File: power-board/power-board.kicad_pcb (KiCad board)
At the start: 2 copper layers, 87.5 x 37.1 mm, 7 parts, among them J1 Conn_01x04_Female, J2 Conn_02x08_Odd_Even, J3 Conn_02x08_Odd_Even, J4 Conn_02x08_Odd_Even, J5 Conn_02x08_Odd_Even, J6 Conn_02x08_Odd_Even, J7 Conn_02x08_Odd_Even

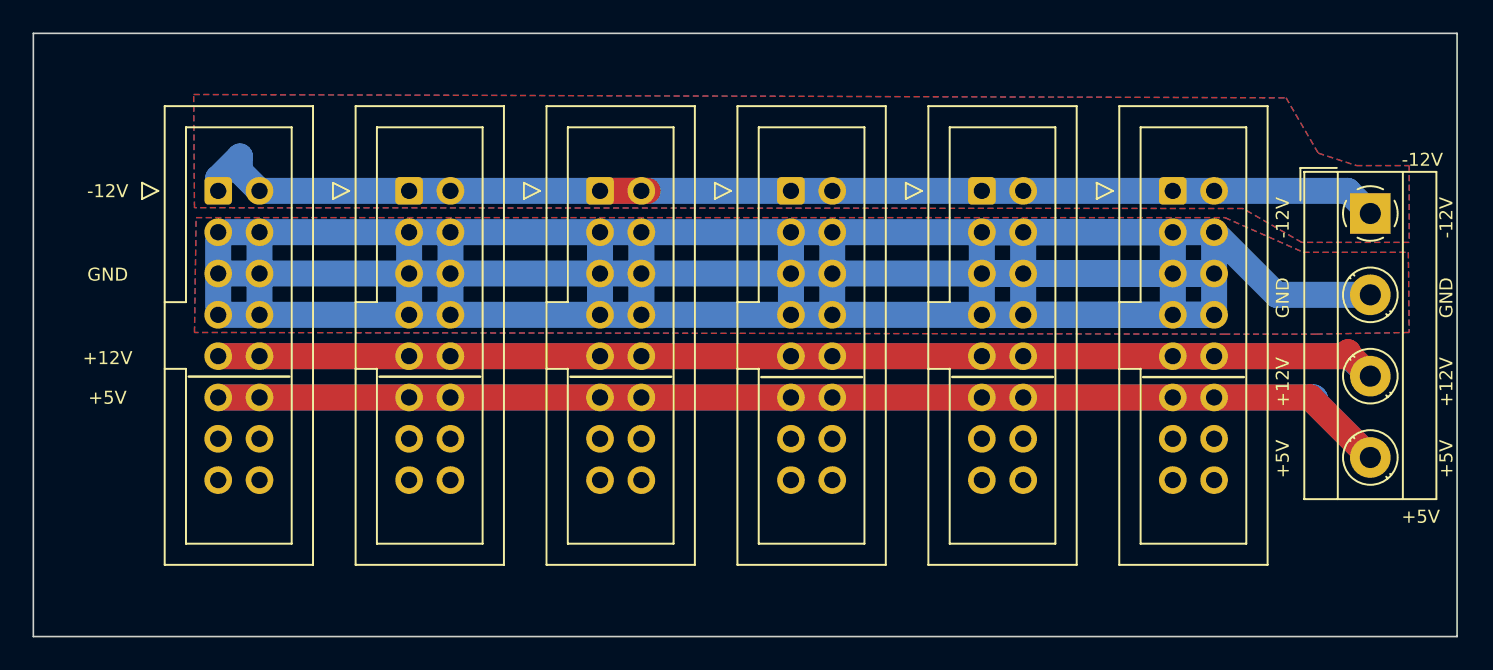
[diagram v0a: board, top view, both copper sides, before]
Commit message: Add mounting holes to power board
And an extra trace connecting the AUX tracks (even though we're not
using them now)
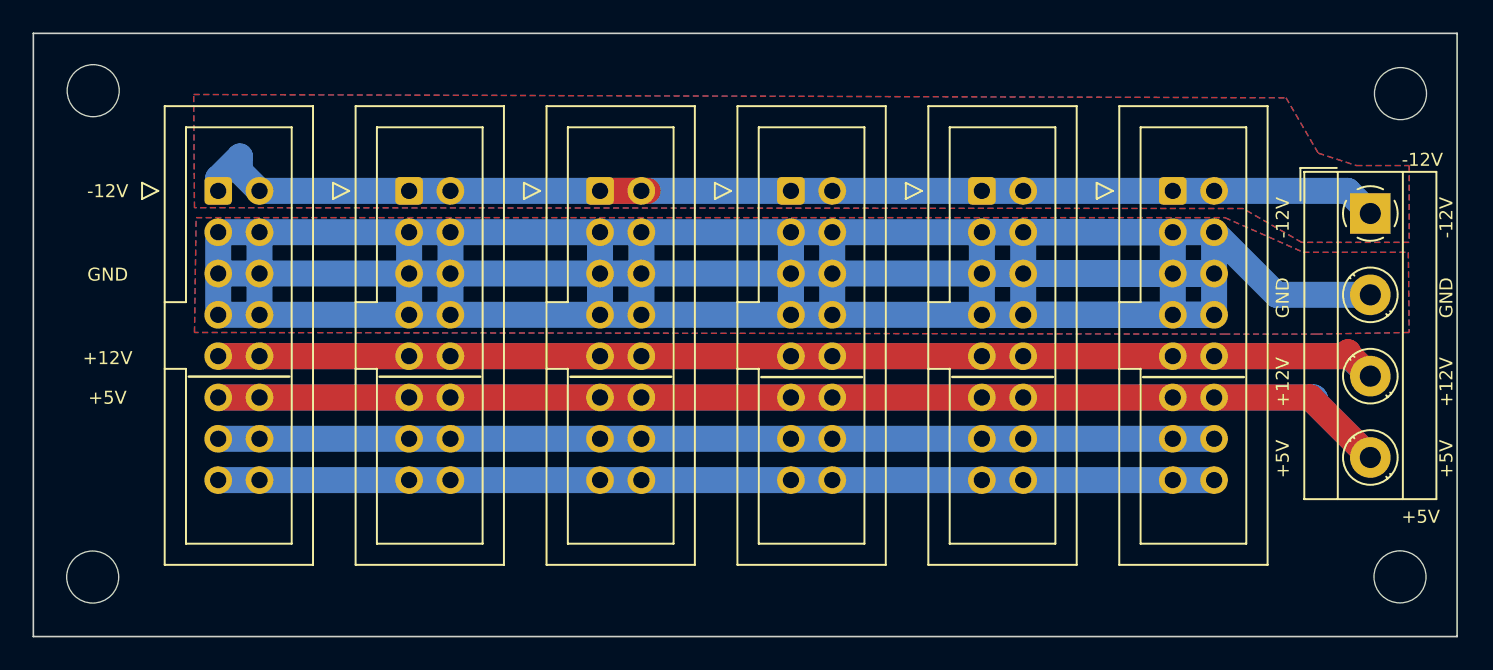
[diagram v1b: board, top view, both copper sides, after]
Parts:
- added REF**: MountingHole_3.2mm_M3_NoCourt, Library:MountingHole_3.2mm_M3_NoCourt, F.Cu at (33.0, 87.7)
- added REF**: MountingHole_3.2mm_M3_NoCourt, Library:MountingHole_3.2mm_M3_NoCourt, F.Cu at (113.4, 58.0)
- added REF**: MountingHole_3.2mm_M3_NoCourt, Library:MountingHole_3.2mm_M3_NoCourt, F.Cu at (33.0, 57.8)
- added REF**: MountingHole_3.2mm_M3_NoCourt, Library:MountingHole_3.2mm_M3_NoCourt, F.Cu at (113.3, 87.7)
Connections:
- J2 pad 13: unconnected-(J2-Pad13) -> Net-(J2-Pad13)
- J2 pad 14: unconnected-(J2-Pad14) -> Net-(J2-Pad13)
- J2 pad 15: unconnected-(J2-Pad15) -> Net-(J2-Pad15)
- J2 pad 16: unconnected-(J2-Pad16) -> Net-(J2-Pad15)
- J3 pad 13: unconnected-(J3-Pad13) -> Net-(J2-Pad13)
- J3 pad 14: unconnected-(J3-Pad14) -> Net-(J2-Pad13)
- J3 pad 15: unconnected-(J3-Pad15) -> Net-(J2-Pad15)
- J3 pad 16: unconnected-(J3-Pad16) -> Net-(J2-Pad15)
- J4 pad 13: unconnected-(J4-Pad13) -> Net-(J2-Pad13)
- J4 pad 14: unconnected-(J4-Pad14) -> Net-(J2-Pad13)
- J4 pad 15: unconnected-(J4-Pad15) -> Net-(J2-Pad15)
- J4 pad 16: unconnected-(J4-Pad16) -> Net-(J2-Pad15)
- J5 pad 13: unconnected-(J5-Pad13) -> Net-(J2-Pad13)
- J5 pad 14: unconnected-(J5-Pad14) -> Net-(J2-Pad13)
- J5 pad 15: unconnected-(J5-Pad15) -> Net-(J2-Pad15)
- J5 pad 16: unconnected-(J5-Pad16) -> Net-(J2-Pad15)
- J6 pad 13: unconnected-(J6-Pad13) -> Net-(J2-Pad13)
- J6 pad 14: unconnected-(J6-Pad14) -> Net-(J2-Pad13)
- J6 pad 15: unconnected-(J6-Pad15) -> Net-(J2-Pad15)
- J6 pad 16: unconnected-(J6-Pad16) -> Net-(J2-Pad15)
- J7 pad 13: unconnected-(J7-Pad13) -> Net-(J2-Pad13)
- J7 pad 14: unconnected-(J7-Pad14) -> Net-(J2-Pad13)
- J7 pad 15: unconnected-(J7-Pad15) -> Net-(J2-Pad15)
- J7 pad 16: unconnected-(J7-Pad16) -> Net-(J2-Pad15)
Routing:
- net Net-(J2-Pad15): track 0.00 -> 61.2 mm
- net Net-(J2-Pad13): track 0.00 -> 61.2 mm
